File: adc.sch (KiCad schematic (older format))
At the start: 64 parts, among them U10 1.5k, U35 MCP6004, U36 MCP6004, U37 10k, U38 10k, U39 10nF, U40 10nF, U41 1k, U42 1k, U43 1.5k, U44 1.5k, U46 MCP6004, U48 10k, U50 10nF, U52 1k, U54 1.5k, U6 10k, U7 10nF, U8 MCP6004, U9 1k

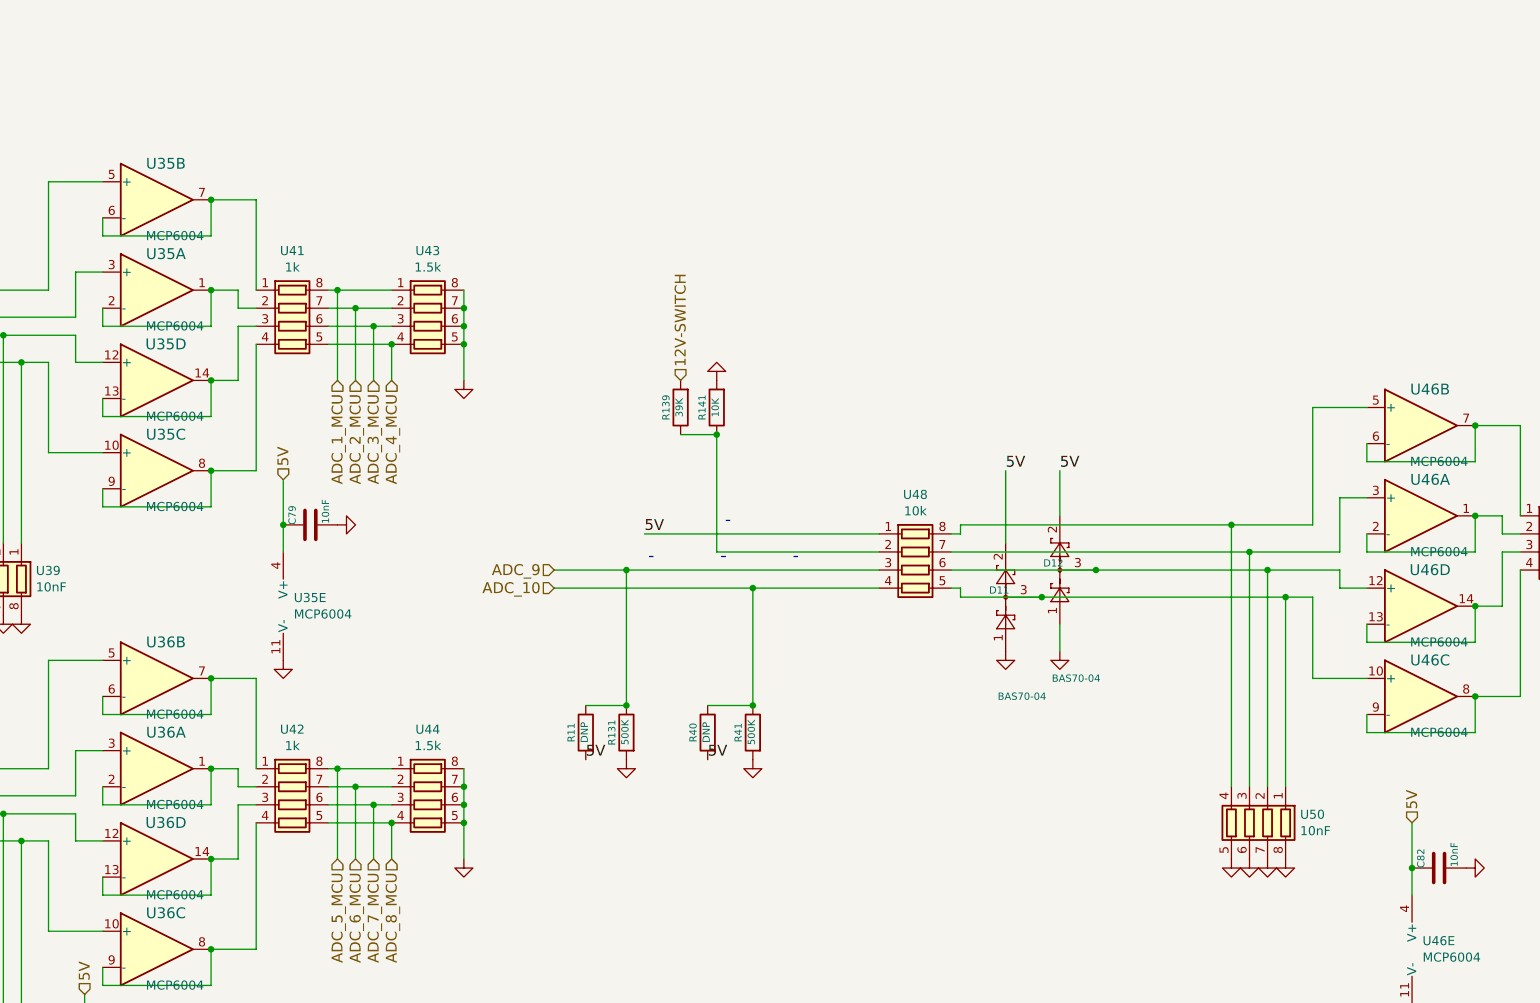
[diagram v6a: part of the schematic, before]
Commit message: from Ola and Jared (#71)
* Update

* removed fp-info-cache from git

* Gerbers

* moved connector

* Mostly Ola's e-mailed copy, plus some of my own fixes to his almost done revision. I also did some house cleaning, with boundary edges, removed most DRC and ERC errors, etc.

* added Fiducial's
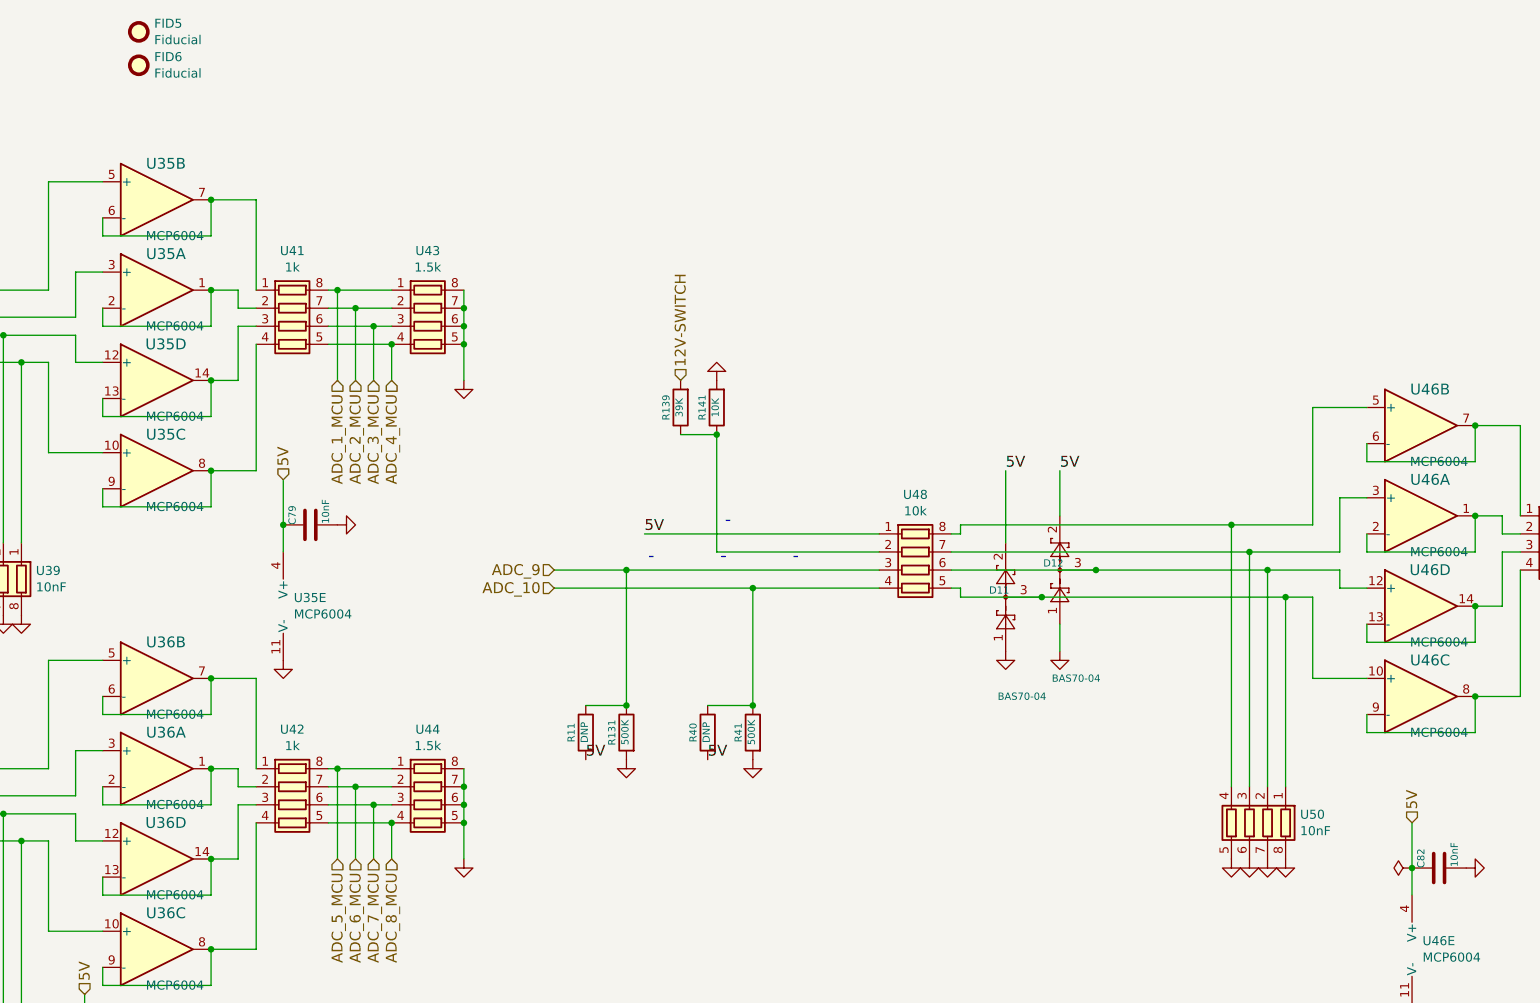
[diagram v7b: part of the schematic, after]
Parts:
- added FID5, FID6: Fiducial, Fiducial:Fiducial_0.5mm_Mask1mm, symbol Mechanical:Fiducial
- C40, C41, C79, C80, C82: footprint Capacitor_SMD:C_0603_1608Metric_Pad1.05x0.95mm_HandSolder -> Capacitor_SMD:C_0603_1608Metric
- R11, R131, R139, R14, R141, R23, R24, R25, R27, R28, R30, R31, R32, R34, R35, R37, R38, R39, R40, R41, R52, R54, R56, R58: footprint Resistor_SMD:R_0603_1608Metric_Pad1.05x0.95mm_HandSolder -> Resistor_SMD:R_0603_1608Metric
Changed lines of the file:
@@
 encoding utf-8
 Sheet 5 7
-Title "frankenso"
-Date "2018-02-24"
-Rev "0.5.3"
+Title "microRusEfi"
+Date "2019-07-01"
+Rev "R0.2"
 Comp "rusEFI.com"
 Comment1 ""
@@
 F 0 "C79" H 7500 3450 40  0000 L CNN
 F 1 "10nF" H 7506 3265 40  0000 L CNN
-F 2 "Capacitor_SMD:C_0603_1608Metric_Pad1.05x0.95mm_HandSolder" V 4130 -2300 60  0001 C CNN
+F 2 "Capacitor_SMD:C_0603_1608Metric" V 4130 -2300 60  0001 C CNN
 F 3 "" H 7500 3350 60  0001 C CNN
 	1    7500 3350
@@
 F 0 "R131" V 9330 4500 40  0000 C CNN
 F 1 "500K" V 9257 4501 40  0000 C CNN
-F 2 "Resistor_SMD:R_0603_1608Metric_Pad1.05x0.95mm_HandSolder" V 11055 3700 60  0001 C CNN
+F 2 "Resistor_SMD:R_0603_1608Metric" V 11055 3700 60  0001 C CNN
 F 3 "" H 14575 3725 60  0001 C CNN
 	1    9250 4500
@@
 F 0 "C80" H 6400 6300 40  0000 L CNN
 F 1 "10nF" H 6406 6115 40  0000 L CNN
-F 2 "Capacitor_SMD:C_0603_1608Metric_Pad1.05x0.95mm_HandSolder" V 3030 550 60  0001 C CNN
+F 2 "Capacitor_SMD:C_0603_1608Metric" V 3030 550 60  0001 C CNN
 F 3 "" H 6400 6200 60  0001 C CNN
 	1    6400 6200
@@
 F 0 "R139" V 9630 2700 40  0000 C CNN
 F 1 "39K" V 9557 2701 40  0000 C CNN
-F 2 "Resistor_SMD:R_0603_1608Metric_Pad1.05x0.95mm_HandSolder" V 11355 2400 60  0001 C CNN
+F 2 "Resistor_SMD:R_0603_1608Metric" V 11355 2400 60  0001 C CNN
 F 3 "" H 14875 2425 60  0001 C CNN
 	1    9550 2700
@@
 F 0 "R141" V 9830 2700 40  0000 C CNN
 F 1 "10K" V 9757 2701 40  0000 C CNN
-F 2 "Resistor_SMD:R_0603_1608Metric_Pad1.05x0.95mm_HandSolder" V 11555 1900 60  0001 C CNN
+F 2 "Resistor_SMD:R_0603_1608Metric" V 11555 1900 60  0001 C CNN
 F 3 "" H 15075 1925 60  0001 C CNN
 	1    9750 2700
@@
 F 0 "C82" H 13750 5350 40  0000 L CNN
 F 1 "10nF" H 13756 5165 40  0000 L CNN
-F 2 "Capacitor_SMD:C_0603_1608Metric_Pad1.05x0.95mm_HandSolder" V 10380 -400 60  0001 C CNN
+F 2 "Capacitor_SMD:C_0603_1608Metric" V 10380 -400 60  0001 C CNN
 F 3 "" H 13750 5250 60  0001 C CNN
 	1    13750 5250
@@
 F 0 "R14" V 2580 1450 40  0000 C CNN
 F 1 "2.7K" V 2507 1451 40  0000 C CNN
-F 2 "Resistor_SMD:R_0603_1608Metric_Pad1.05x0.95mm_HandSolder" V 4305 1150 60  0001 C CNN
+F 2 "Resistor_SMD:R_0603_1608Metric" V 4305 1150 60  0001 C CNN
 F 3 "" H 7825 1175 60  0001 C CNN
 	1    2500 1450
@@
 F 0 "R23" V 2755 1450 40  0000 C CNN
 F 1 "2.7K" V 2682 1451 40  0000 C CNN
-F 2 "Resistor_SMD:R_0603_1608Metric_Pad1.05x0.95mm_HandSolder" V 4480 1150 60  0001 C CNN
+F 2 "Resistor_SMD:R_0603_1608Metric" V 4480 1150 60  0001 C CNN
 F 3 "" H 8000 1175 60  0001 C CNN
 	1    2675 1450
@@
 F 0 "R25" V 2930 1450 40  0000 C CNN
 F 1 "2.7K" V 2857 1451 40  0000 C CNN
-F 2 "Resistor_SMD:R_0603_1608Metric_Pad1.05x0.95mm_HandSolder" V 4655 1150 60  0001 C CNN
+F 2 "Resistor_SMD:R_0603_1608Metric" V 4655 1150 60  0001 C CNN
 F 3 "" H 8175 1175 60  0001 C CNN
 	1    2850 1450
@@
 F 0 "R27" V 3105 1450 40  0000 C CNN
 F 1 "2.7K" V 3032 1451 40  0000 C CNN
-F 2 "Resistor_SMD:R_0603_1608Metric_Pad1.05x0.95mm_HandSolder" V 4830 1150 60  0001 C CNN
+F 2 "Resistor_SMD:R_0603_1608Metric" V 4830 1150 60  0001 C CNN
 F 3 "" H 8350 1175 60  0001 C CNN
 	1    3025 1450
@@
 F 0 "R11" V 9105 4500 40  0000 C CNN
 F 1 "DNP" V 9032 4501 40  0000 C CNN
-F 2 "Resistor_SMD:R_0603_1608Metric_Pad1.05x0.95mm_HandSolder" V 10830 4200 60  0001 C CNN
+F 2 "Resistor_SMD:R_0603_1608Metric" V 10830 4200 60  0001 C CNN
 F 3 "" H 14350 4225 60  0001 C CNN
 	1    9025 4500
@@
 F 0 "R41" V 10030 4500 40  0000 C CNN
 F 1 "500K" V 9957 4501 40  0000 C CNN
-F 2 "Resistor_SMD:R_0603_1608Metric_Pad1.05x0.95mm_HandSolder" V 11755 3700 60  0001 C CNN
+F 2 "Resistor_SMD:R_0603_1608Metric" V 11755 3700 60  0001 C CNN
 F 3 "" H 15275 3725 60  0001 C CNN
 	1    9950 4500
@@
 F 0 "R38" V 2930 2775 40  0000 C CNN
 F 1 "500K" V 2857 2776 40  0000 C CNN
-F 2 "Resistor_SMD:R_0603_1608Metric_Pad1.05x0.95mm_HandSolder" V 4655 1975 60  0001 C CNN
+F 2 "Resistor_SMD:R_0603_1608Metric" V 4655 1975 60  0001 C CNN
 F 3 "" H 8175 2000 60  0001 C CNN
 	1    2850 2775
@@
 F 0 "R35" V 2755 2775 40  0000 C CNN
 F 1 "500K" V 2682 2776 40  0000 C CNN
-F 2 "Resistor_SMD:R_0603_1608Metric_Pad1.05x0.95mm_HandSolder" V 4480 1975 60  0001 C CNN
+F 2 "Resistor_SMD:R_0603_1608Metric" V 4480 1975 60  0001 C CNN
 F 3 "" H 8000 2000 60  0001 C CNN
 	1    2675 2775
@@
 F 0 "R32" V 2580 2775 40  0000 C CNN
 F 1 "500K" V 2507 2776 40  0000 C CNN
-F 2 "Resistor_SMD:R_0603_1608Metric_Pad1.05x0.95mm_HandSolder" V 4305 1975 60  0001 C CNN
+F 2 "Resistor_SMD:R_0603_1608Metric" V 4305 1975 60  0001 C CNN
 F 3 "" H 7825 2000 60  0001 C CNN
 	1    2500 2775
@@
 F 0 "R39" V 3105 2775 40  0000 C CNN
 F 1 "500K" V 3032 2776 40  0000 C CNN
-F 2 "Resistor_SMD:R_0603_1608Metric_Pad1.05x0.95mm_HandSolder" V 4830 1975 60  0001 C CNN
+F 2 "Resistor_SMD:R_0603_1608Metric" V 4830 1975 60  0001 C CNN
 F 3 "" H 8350 2000 60  0001 C CNN
 	1    3025 2775
@@
 F 0 "R34" V 2605 5425 40  0000 C CNN
 F 1 "500K" V 2532 5426 40  0000 C CNN
-F 2 "Resistor_SMD:R_0603_1608Metric_Pad1.05x0.95mm_HandSolder" V 4330 4625 60  0001 C CNN
+F 2 "Resistor_SMD:R_0603_1608Metric" V 4330 4625 60  0001 C CNN
 F 3 "" H 7850 4650 60  0001 C CNN
 	1    2525 5425
@@
 F 0 "R31" V 2430 5425 40  0000 C CNN
 F 1 "500K" V 2357 5426 40  0000 C CNN
-F 2 "Resistor_SMD:R_0603_1608Metric_Pad1.05x0.95mm_HandSolder" V 4155 4625 60  0001 C CNN
+F 2 "Resistor_SMD:R_0603_1608Metric" V 4155 4625 60  0001 C CNN
 F 3 "" H 7675 4650 60  0001 C CNN
 	1    2350 5425
@@
 F 0 "R24" V 2255 5425 40  0000 C CNN
 F 1 "500K" V 2182 5426 40  0000 C CNN
-F 2 "Resistor_SMD:R_0603_1608Metric_Pad1.05x0.95mm_HandSolder" V 3980 4625 60  0001 C CNN
+F 2 "Resistor_SMD:R_0603_1608Metric" V 3980 4625 60  0001 C CNN
 F 3 "" H 7500 4650 60  0001 C CNN
 	1    2175 5425
@@
 F 0 "R37" V 2780 5425 40  0000 C CNN
 F 1 "500K" V 2707 5426 40  0000 C CNN
-F 2 "Resistor_SMD:R_0603_1608Metric_Pad1.05x0.95mm_HandSolder" V 4505 4625 60  0001 C CNN
+F 2 "Resistor_SMD:R_0603_1608Metric" V 4505 4625 60  0001 C CNN
 F 3 "" H 8025 4650 60  0001 C CNN
 	1    2700 5425
@@
 F 0 "R40" V 9780 4500 40  0000 C CNN
 F 1 "DNP" V 9707 4501 40  0000 C CNN
-F 2 "Resistor_SMD:R_0603_1608Metric_Pad1.05x0.95mm_HandSolder" V 11505 4200 60  0001 C CNN
+F 2 "Resistor_SMD:R_0603_1608Metric" V 11505 4200 60  0001 C CNN
 F 3 "" H 15025 4225 60  0001 C CNN
 	1    9700 4500
@@
 F 0 "C40" H 7050 9700 40  0000 L CNN
 F 1 "10nF" H 7056 9515 40  0000 L CNN
-F 2 "Capacitor_SMD:C_0603_1608Metric_Pad1.05x0.95mm_HandSolder" V 3680 3950 60  0001 C CNN
+F 2 "Capacitor_SMD:C_0603_1608Metric" V 3680 3950 60  0001 C CNN
 F 3 "" H 7050 9600 60  0001 C CNN
 	1    7050 9600
@@
 F 0 "R56" V 2480 9025 40  0000 C CNN
 F 1 "500K" V 2407 9026 40  0000 C CNN
-F 2 "Resistor_SMD:R_0603_1608Metric_Pad1.05x0.95mm_HandSolder" V 4205 8225 60  0001 C CNN
+F 2 "Resistor_SMD:R_0603_1608Metric" V 4205 8225 60  0001 C CNN
 F 3 "" H 7725 8250 60  0001 C CNN
 	1    2400 9025
@@
 F 0 "R54" V 2305 9025 40  0000 C CNN
 F 1 "500K" V 2232 9026 40  0000 C CNN
-F 2 "Resistor_SMD:R_0603_1608Metric_Pad1.05x0.95mm_HandSolder" V 4030 8225 60  0001 C CNN
+F 2 "Resistor_SMD:R_0603_1608Metric" V 4030 8225 60  0001 C CNN
 F 3 "" H 7550 8250 60  0001 C CNN
 	1    2225 9025
@@
 F 0 "R52" V 2130 9025 40  0000 C CNN
 F 1 "500K" V 2057 9026 40  0000 C CNN
-F 2 "Resistor_SMD:R_0603_1608Metric_Pad1.05x0.95mm_HandSolder" V 3855 8225 60  0001 C CNN
+F 2 "Resistor_SMD:R_0603_1608Metric" V 3855 8225 60  0001 C CNN
 F 3 "" H 7375 8250 60  0001 C CNN
 	1    2050 9025
@@
 F 0 "R58" V 2655 9025 40  0000 C CNN
 F 1 "500K" V 2582 9026 40  0000 C CNN
-F 2 "Resistor_SMD:R_0603_1608Metric_Pad1.05x0.95mm_HandSolder" V 4380 8225 60  0001 C CNN
+F 2 "Resistor_SMD:R_0603_1608Metric" V 4380 8225 60  0001 C CNN
 F 3 "" H 7900 8250 60  0001 C CNN
 	1    2575 9025
@@
 F 0 "R28" V 10580 7075 40  0000 C CNN
 F 1 "2.15K" V 10507 7076 40  0000 C CNN
-F 2 "Resistor_SMD:R_0603_1608Metric_Pad1.05x0.95mm_HandSolder" V 12305 6275 60  0001 C CNN
+F 2 "Resistor_SMD:R_0603_1608Metric" V 12305 6275 60  0001 C CNN
 F 3 "" H 15825 6300 60  0001 C CNN
 	1    10500 7075
@@
 F 0 "R30" V 10855 7225 40  0000 C CNN
 F 1 "33K" V 10782 7226 40  0000 C CNN
-F 2 "Resistor_SMD:R_0603_1608Metric_Pad1.05x0.95mm_HandSolder" V 12580 6425 60  0001 C CNN
+F 2 "Resistor_SMD:R_0603_1608Metric" V 12580 6425 60  0001 C CNN
 F 3 "" H 16100 6450 60  0001 C CNN
 	1    10775 7225
@@
 F 0 "C41" H 10975 7475 40  0000 L CNN
 F 1 "1nF" H 10981 7290 40  0000 L CNN
-F 2 "Capacitor_SMD:C_0603_1608Metric_Pad1.05x0.95mm_HandSolder" V 7605 1725 60  0001 C CNN
+F 2 "Capacitor_SMD:C_0603_1608Metric" V 7605 1725 60  0001 C CNN
 F 3 "" H 10975 7375 60  0001 C CNN
 	1    10975 7375
@@
 Wire Wire Line
 	11500 7225 11650 7225
+$Comp
+L power:PWR_FLAG #FLG0104
+U 1 1 5D32079B
+P 13600 5250
+F 0 "#FLG0104" H 13600 5325 50  0001 C CNN
+F 1 "PWR_FLAG" V 13600 5377 50  0001 L CNN
+F 2 "" H 13600 5250 50  0001 C CNN
+F 3 "~" H 13600 5250 50  0001 C CNN
+	1    13600 5250
+	0    -1   -1   0
+$EndComp
+$Comp
+L Mechanical:Fiducial FID5
+U 1 1 5D1FF61B
+P 6550 620
+F 0 "FID5" H 6635 666 50  0000 L CNN
+F 1 "Fiducial" H 6635 575 50  0000 L CNN
+F 2 "Fiducial:Fiducial_0.5mm_Mask1mm" H 6550 620 50  0001 C CNN
+F 3 "~" H 6550 620 50  0001 C CNN
+	1    6550 620
+	1    0    0    -1
+$EndComp
+$Comp
+L Mechanical:Fiducial FID6
+U 1 1 5D20808D
+P 6550 805
+F 0 "FID6" H 6635 851 50  0000 L CNN
+F 1 "Fiducial" H 6635 760 50  0000 L CNN
+F 2 "Fiducial:Fiducial_0.5mm_Mask1mm" H 6550 805 50  0001 C CNN
+F 3 "~" H 6550 805 50  0001 C CNN
+	1    6550 805
+	1    0    0    -1
+$EndComp
 $EndSCHEMATC

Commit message: Updated logo symbol and footprint, BOM is 99% entered in KC schematic now.
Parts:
- C40, C79, C80, C82: Manufacturer (none) -> KEMET; Part # (none) -> C0603C103K1RACTU; VEND (none) -> DIGI; VEND# (none) -> 399-3189-1-ND
- C41: Manufacturer (none) -> MURATA; Part # (none) -> GRM1885C1H102FA01D; VEND (none) -> DIGI; VEND# (none) -> 490-6377-1-ND
- D10, D11, D12, D13, D18, D24, D25, D26, D3, D4, D5, D6, D7, D8, D9: Manufacturer (none) -> ON-SEMI; Part # BAS70-04 -> SBAS70-04LT1G; VEND (none) -> DIGI; VEND# (none) -> SBAS70-04LT1GOSCT-ND
- FID5, FID6: Manufacturer (none) -> DNP; Part # (none) -> DNP; VEND (none) -> DNP; VEND# (none) -> DNP
- R11, R40: Manufacturer (none) -> DNP; Part # (none) -> DNP; VEND (none) -> DIGI; VEND# (none) -> DNP
- R131, R24, R31, R32, R34, R35, R37, R38, R39, R41, R52, R54, R56, R58: Manufacturer (none) -> StackPole; Part # (none) -> RMCF0603FT470K; VEND (none) -> DIGI; VEND# (none) -> RMCF0603FT470KCT-ND
- R139: Manufacturer (none) -> Yageo; Part # (none) -> RC0603FR-0739KL; VEND (none) -> DIGI; VEND# (none) -> 311-39.0KHRCT-ND
- R14, R23, R25, R27: Manufacturer (none) -> StackPole; Part # (none) -> RMCF0603JT2K70; VEND (none) -> DIGI; VEND# (none) -> RMCF0603JT2K70CT-ND
- R141: Manufacturer (none) -> StackPole; Part # (none) -> RMCF0603JT10K0; VEND (none) -> DIGI; VEND# (none) -> RMCF0603JT10K0CT-ND
- R28: Manufacturer (none) -> mm; Part # (none) -> dd; VEND (none) -> DIGI; VEND# (none) -> vv
- R30: Manufacturer (none) -> StackPole; Part # (none) -> RMCF0603JT33K0; VEND (none) -> DIGI; VEND# (none) -> RMCF0603JT33K0CT-ND
- U10, U43, U44, U54: Manufacturer (none) -> Panasonic; VEND (none) -> DIGI; VEND# (none) -> Y4152CT-ND
- U35, U36, U46, U8: Manufacturer (none) -> MicroChip; Part # 579-MCP6004T-I/ST -> MCP6004T-I/ST; VEND (none) -> DIGI; VEND# 579-MCP6004T-I/ST -> MCP6004T-I/STCT-ND
- U37, U38, U48, U6: Manufacturer (none) -> Yageo; VEND (none) -> DIGI; VEND# 603-YC324-JK-0710KL -> YC324J-10KCT-ND
- U39, U40, U50, U7: Manufacturer (none) -> KEMET; Part # 80-CA064X103K2RAUTO -> CA064X103K2RACAUTO; VEND (none) -> DIGI; VEND# (none) -> 399-12382-1-ND
- U41, U42, U52, U9: Manufacturer (none) -> Panasonic; Part # 667-EXB-V8V102JV -> EXB-V8V102JV; VEND (none) -> DIGI; VEND# 667-EXB-V8V102JV -> Y4102CT-ND
